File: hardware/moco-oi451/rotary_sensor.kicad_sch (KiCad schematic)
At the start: 2 parts, among them U5 AS5047x

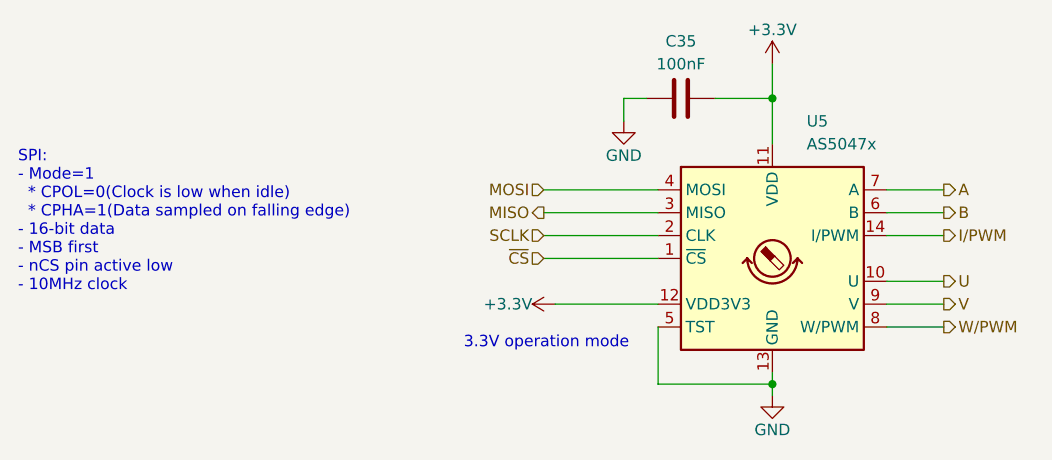
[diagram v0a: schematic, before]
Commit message: Optimize routing
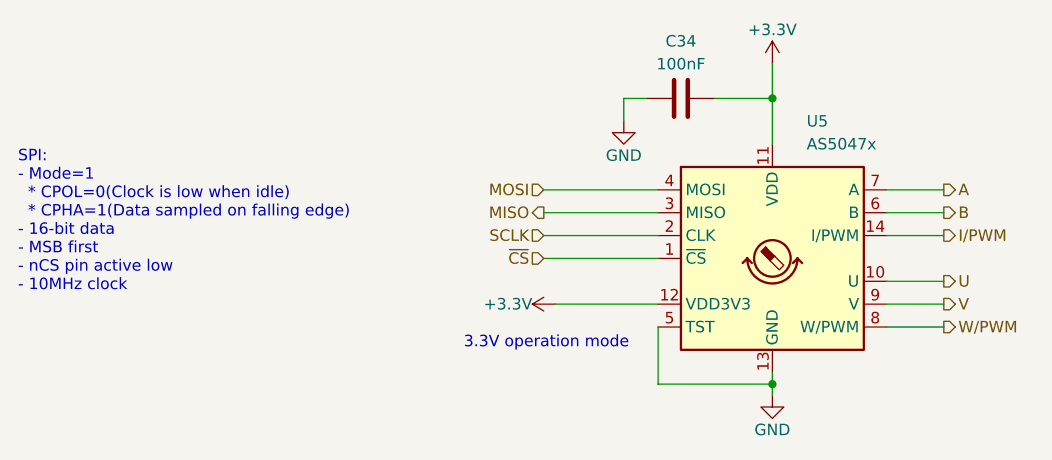
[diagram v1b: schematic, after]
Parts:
- renumbered C35 to C34
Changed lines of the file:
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@@
   (symbol (lib_id "power:GND") (at 127 85.09 0) (unit 1)
     (in_bom yes) (on_board yes) (dnp no)
-    (property "Reference" "#PWR040" (at 127 91.44 0)
+    (property "Reference" "#PWR039" (at 127 91.44 0)
       (effects (font (size 1.27 1.27)) hide)
     )
@@
     )
     (property "Datasheet" "" (at 127 85.09 0)
+      (effects (font (size 1.27 1.27)) hide)
+    )
+    (pin "1")
+    (instances
+      (project "moco-oi451"
+        (path "/171831cd-2a0d-47b9-8420-65898c688d08/09f9ddc7-dce7-4d23-abae-17b64541c78f"
+          (reference "#PWR039") (unit 1)
+        )
+      )
+      (project "moco-od501"
+        (path "/6af178d2-5089-4f26-a9dd-467044aa844a/114d852e-094a-459a-bc11-aa9bc2294143"
+          (reference "#PWR?") (unit 1)
+        )
+      )
+    )
+  )
+  (symbol (lib_id "Device:C") (at 133.35 82.55 90) (unit 1)
+    (in_bom yes) (on_board yes) (dnp no)
+    (property "Reference" "C34" (at 133.35 76.2 90)
+      (effects (font (size 1.27 1.27)))
+    )
+    (property "Value" "100nF" (at 133.35 78.74 90)
+      (effects (font (size 1.27 1.27)))
+    )
+    (property "Footprint" "Capacitor_SMD:C_0603_1608Metric_Pad1.08x0.95mm_HandSolder" (at 137.16 81.5848 0)
+      (effects (font (size 1.27 1.27)) hide)
+    )
+    (property "Datasheet" "~" (at 133.35 82.55 0)
+      (effects (font (size 1.27 1.27)) hide)
+    )
+    (pin "1")
+    (pin "2")
+    (instances
+      (project "moco-oi451"
+        (path "/171831cd-2a0d-47b9-8420-65898c688d08/09f9ddc7-dce7-4d23-abae-17b64541c78f"
+          (reference "C34") (unit 1)
+        )
+      )
+    )
+  )
+  (symbol (lib_id "power:GND") (at 143.51 115.57 0) (unit 1)
+    (in_bom yes) (on_board yes) (dnp no)
+    (property "Reference" "#PWR041" (at 143.51 121.92 0)
+      (effects (font (size 1.27 1.27)) hide)
+    )
+    (property "Value" "GND" (at 143.51 119.38 0)
+      (effects (font (size 1.27 1.27)))
+    )
+    (property "Footprint" "" (at 143.51 115.57 0)
+      (effects (font (size 1.27 1.27)) hide)
+    )
+    (property "Datasheet" "" (at 143.51 115.57 0)
+      (effects (font (size 1.27 1.27)) hide)
+    )
+    (pin "1")
+    (instances
+      (project "moco-oi451"
+        (path "/171831cd-2a0d-47b9-8420-65898c688d08/09f9ddc7-dce7-4d23-abae-17b64541c78f"
+          (reference "#PWR041") (unit 1)
+        )
+      )
+      (project "moco-od501"
+        (path "/6af178d2-5089-4f26-a9dd-467044aa844a/114d852e-094a-459a-bc11-aa9bc2294143"
+          (reference "#PWR?") (unit 1)
+        )
+      )
+    )
+  )
+  (symbol (lib_id "power:+3.3V") (at 119.38 105.41 90) (unit 1)
+    (in_bom yes) (on_board yes) (dnp no)
+    (property "Reference" "#PWR040" (at 123.19 105.41 0)
+      (effects (font (size 1.27 1.27)) hide)
+    )
+    (property "Value" "+3.3V" (at 116.84 105.41 90)
+      (effects (font (size 1.27 1.27)) (justify left))
+    )
+    (property "Footprint" "" (at 119.38 105.41 0)
+      (effects (font (size 1.27 1.27)) hide)
+    )
+    (property "Datasheet" "" (at 119.38 105.41 0)
       (effects (font (size 1.27 1.27)) hide)
     )
@@
     )
   )
-  (symbol (lib_id "Device:C") (at 133.35 82.55 90) (unit 1)
-    (in_bom yes) (on_board yes) (dnp no)
-    (property "Reference" "C35" (at 133.35 76.2 90)
-      (effects (font (size 1.27 1.27)))
-    )
-    (property "Value" "100nF" (at 133.35 78.74 90)
-      (effects (font (size 1.27 1.27)))
-    )
-    (property "Footprint" "Capacitor_SMD:C_0603_1608Metric_Pad1.08x0.95mm_HandSolder" (at 137.16 81.5848 0)
-      (effects (font (size 1.27 1.27)) hide)
-    )
-    (property "Datasheet" "~" (at 133.35 82.55 0)
-      (effects (font (size 1.27 1.27)) hide)
-    )
-    (pin "1")
-    (pin "2")
-    (instances
-      (project "moco-oi451"
-        (path "/171831cd-2a0d-47b9-8420-65898c688d08/09f9ddc7-dce7-4d23-abae-17b64541c78f"
-          (reference "C35") (unit 1)
-        )
-      )
-    )
-  )
-  (symbol (lib_id "power:GND") (at 143.51 115.57 0) (unit 1)
-    (in_bom yes) (on_board yes) (dnp no)
-    (property "Reference" "#PWR042" (at 143.51 121.92 0)
-      (effects (font (size 1.27 1.27)) hide)
-    )
-    (property "Value" "GND" (at 143.51 119.38 0)
-      (effects (font (size 1.27 1.27)))
-    )
-    (property "Footprint" "" (at 143.51 115.57 0)
-      (effects (font (size 1.27 1.27)) hide)
-    )
-    (property "Datasheet" "" (at 143.51 115.57 0)
-      (effects (font (size 1.27 1.27)) hide)
-    )
-    (pin "1")
-    (instances
-      (project "moco-oi451"
-        (path "/171831cd-2a0d-47b9-8420-65898c688d08/09f9ddc7-dce7-4d23-abae-17b64541c78f"
-          (reference "#PWR042") (unit 1)
-        )
-      )
-      (project "moco-od501"
-        (path "/6af178d2-5089-4f26-a9dd-467044aa844a/114d852e-094a-459a-bc11-aa9bc2294143"
-          (reference "#PWR?") (unit 1)
-        )
-      )
-    )
-  )
-  (symbol (lib_id "power:+3.3V") (at 119.38 105.41 90) (unit 1)
-    (in_bom yes) (on_board yes) (dnp no)
-    (property "Reference" "#PWR041" (at 123.19 105.41 0)
-      (effects (font (size 1.27 1.27)) hide)
-    )
-    (property "Value" "+3.3V" (at 116.84 105.41 90)
-      (effects (font (size 1.27 1.27)) (justify left))
-    )
-    (property "Footprint" "" (at 119.38 105.41 0)
-      (effects (font (size 1.27 1.27)) hide)
-    )
-    (property "Datasheet" "" (at 119.38 105.41 0)
-      (effects (font (size 1.27 1.27)) hide)
-    )
-    (pin "1")
-    (instances
-      (project "moco-oi451"
-        (path "/171831cd-2a0d-47b9-8420-65898c688d08/09f9ddc7-dce7-4d23-abae-17b64541c78f"
-          (reference "#PWR041") (unit 1)
-        )
-      )
-      (project "moco-od501"
-        (path "/6af178d2-5089-4f26-a9dd-467044aa844a/114d852e-094a-459a-bc11-aa9bc2294143"
-          (reference "#PWR?") (unit 1)
-        )
-      )
-    )
-  )
   (symbol (lib_id "power:+3.3V") (at 143.51 78.74 0) (unit 1)
     (in_bom yes) (on_board yes) (dnp no)
-    (property "Reference" "#PWR039" (at 143.51 82.55 0)
+    (property "Reference" "#PWR038" (at 143.51 82.55 0)
       (effects (font (size 1.27 1.27)) hide)
     )
@@
       (project "moco-oi451"
         (path "/171831cd-2a0d-47b9-8420-65898c688d08/09f9ddc7-dce7-4d23-abae-17b64541c78f"
-          (reference "#PWR039") (unit 1)
+          (reference "#PWR038") (unit 1)
         )
       )
